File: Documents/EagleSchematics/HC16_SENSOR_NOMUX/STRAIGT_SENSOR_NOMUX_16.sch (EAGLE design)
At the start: 33 parts

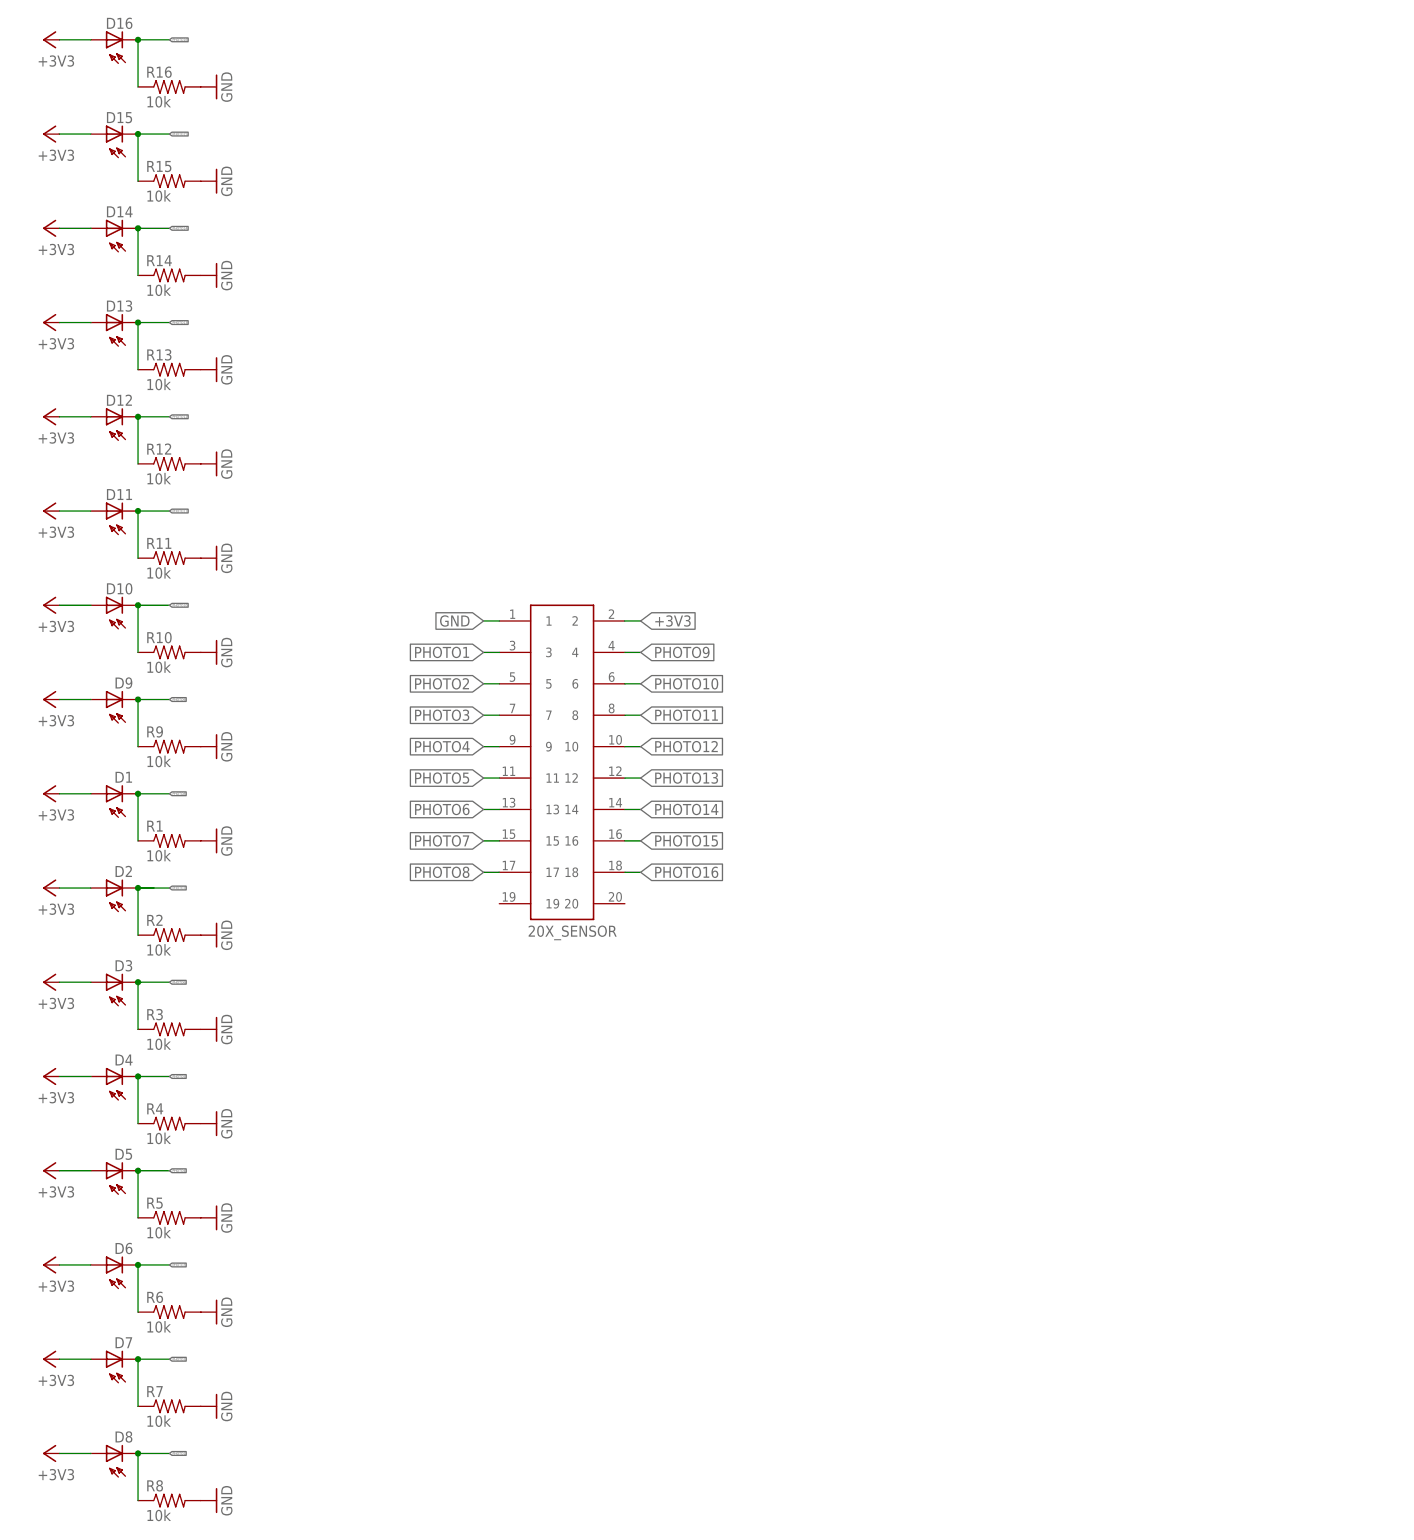
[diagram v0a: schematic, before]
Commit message: Eagle Schematics
Changed array of sensornetwork
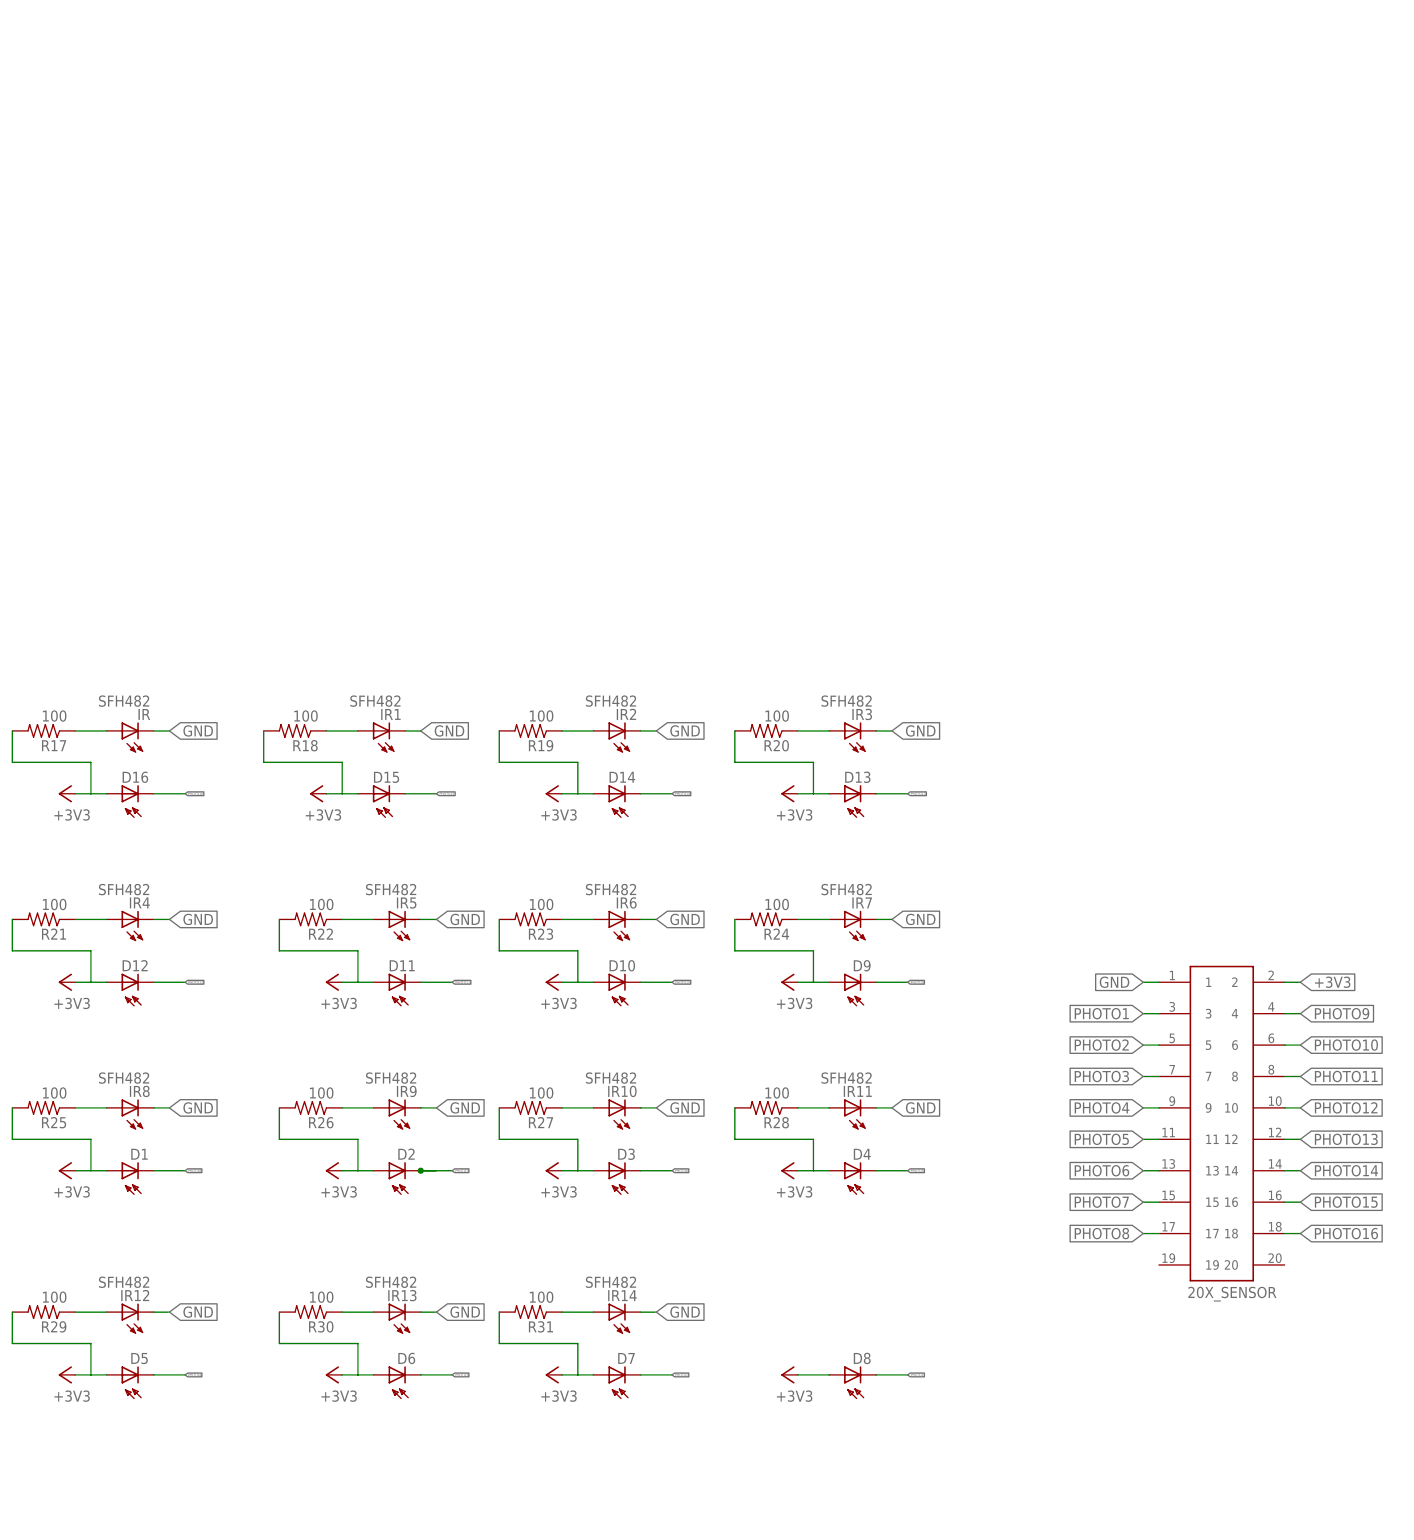
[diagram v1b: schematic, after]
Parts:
- removed R1, R10, R11, R12, R13, R14, R15, R16, R2, R3, R4, R5, R6, R7, R8, R9: 10k, resistor:R-US_0207/10
- added IR, IR1, IR10, IR11, IR12, IR13, IR14, IR2, IR3, IR4, IR5, IR6, IR7, IR8, IR9: SFH482, led:SFH482
- added R17, R18, R19, R20, R21, R22, R23, R24, R25, R26, R27, R28, R29, R30, R31: 100, resistor:R-US_0207/10
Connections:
- new net N$1: IR1.A, R18.1
- new net N$10: IR9.A, R26.1
- new net N$11: IR10.A, R27.1
- new net N$12: IR11.A, R28.1
- new net N$13: IR12.A, R29.1
- new net N$14: IR13.A, R30.1
- new net N$15: IR14.A, R31.1
- new net N$2: IR.A, R17.1
- new net N$3: IR2.A, R19.1
- new net N$4: IR3.A, R20.1
- new net N$5: IR4.A, R21.1
- new net N$6: IR5.A, R22.1
- new net N$7: IR6.A, R23.1
- new net N$8: IR7.A, R24.1
- new net N$9: IR8.A, R25.1
- net +3V3: now also R17.2, R18.2, R19.2, R20.2, R21.2, R22.2, R23.2, R24.2, R25.2, R26.2, R27.2, R28.2, R29.2, R30.2, R31.2
- net GND: now also IR.C, IR1.C, IR10.C, IR11.C, IR12.C, IR13.C, IR14.C, IR2.C, IR3.C, IR4.C, IR5.C, IR6.C, IR7.C, IR8.C, IR9.C; no longer R1.2, R10.2, R11.2, R12.2, R13.2, R14.2, R15.2, R16.2, R2.2, R3.2, R4.2, R5.2, R6.2, R7.2, R8.2, R9.2
- net PHOTO1: no longer R8.1
- net PHOTO10: no longer R10.1
- net PHOTO11: no longer R11.1
- net PHOTO12: no longer R12.1
- net PHOTO13: no longer R13.1
- net PHOTO14: no longer R14.1
- net PHOTO15: no longer R15.1
- net PHOTO16: no longer R16.1
- net PHOTO2: no longer R7.1
- net PHOTO3: no longer R6.1
- net PHOTO4: no longer R5.1
- net PHOTO5: no longer R4.1
- net PHOTO6: no longer R3.1
- net PHOTO7: no longer R2.1
- net PHOTO8: no longer R1.1
- net PHOTO9: no longer R9.1
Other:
- moved on the sheet: 20X_SENSOR, D1, D10, D11, D12, D13, D14, D15, D16, D2, D3, D4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

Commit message: Almost final version of schematics
Updated BigBoard with the new design
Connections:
- new net +5V: 20X_SENSOR.2
- net +3V3: no longer 20X_SENSOR.2
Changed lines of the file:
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@@
 <wire x1="2.54" y1="124.46" x2="2.54" y2="129.54" width="0.1524" layer="91"/>
-</segment>
-<segment>
-<pinref part="20X_SENSOR" gate="G$1" pin="2"/>
-<wire x1="208.28" y1="88.9" x2="210.82" y2="88.9" width="0.1524" layer="91"/>
-<label x="210.82" y="88.9" size="1.778" layer="95" xref="yes"/>
 </segment>
 </net>
@@
 </segment>
 </net>
+<net name="+5V" class="0">
+<segment>
+<pinref part="20X_SENSOR" gate="G$1" pin="2"/>
+<wire x1="208.28" y1="88.9" x2="210.82" y2="88.9" width="0.1524" layer="91"/>
+<label x="210.82" y="88.9" size="1.778" layer="95" xref="yes"/>
+</segment>
+</net>
